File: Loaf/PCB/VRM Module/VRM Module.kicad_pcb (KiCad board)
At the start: 2 copper layers, 7 parts, among them U1 TPS564242DRLR

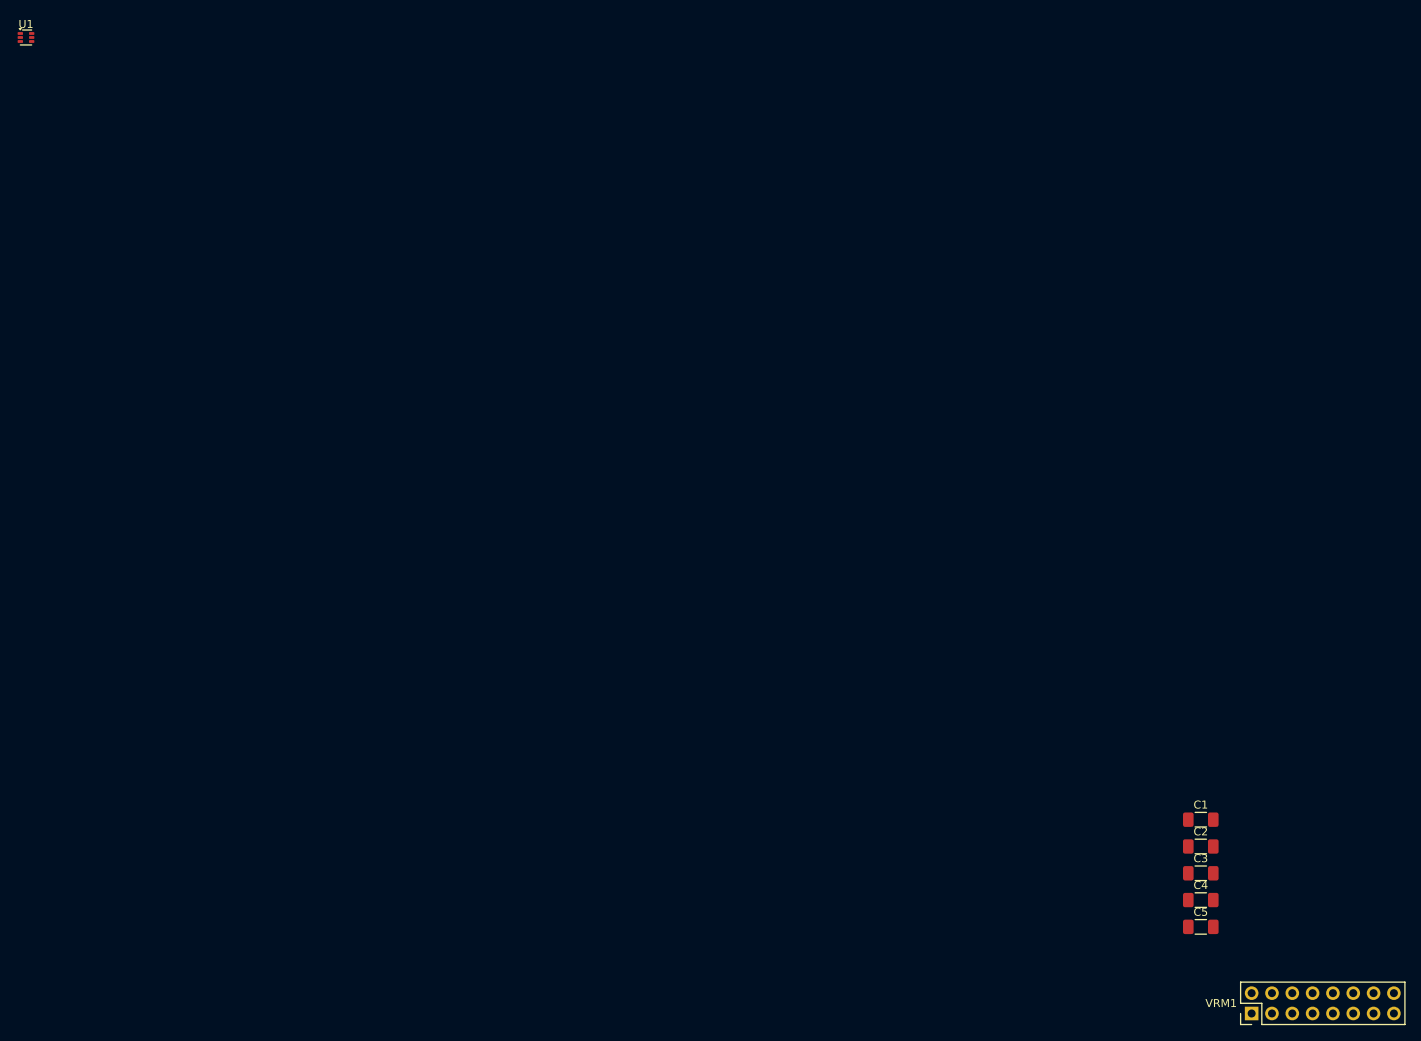
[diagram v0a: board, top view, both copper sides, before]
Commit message: IO PCB redesign progress upload
Switching to pi pico for better performance and to keep UART interface
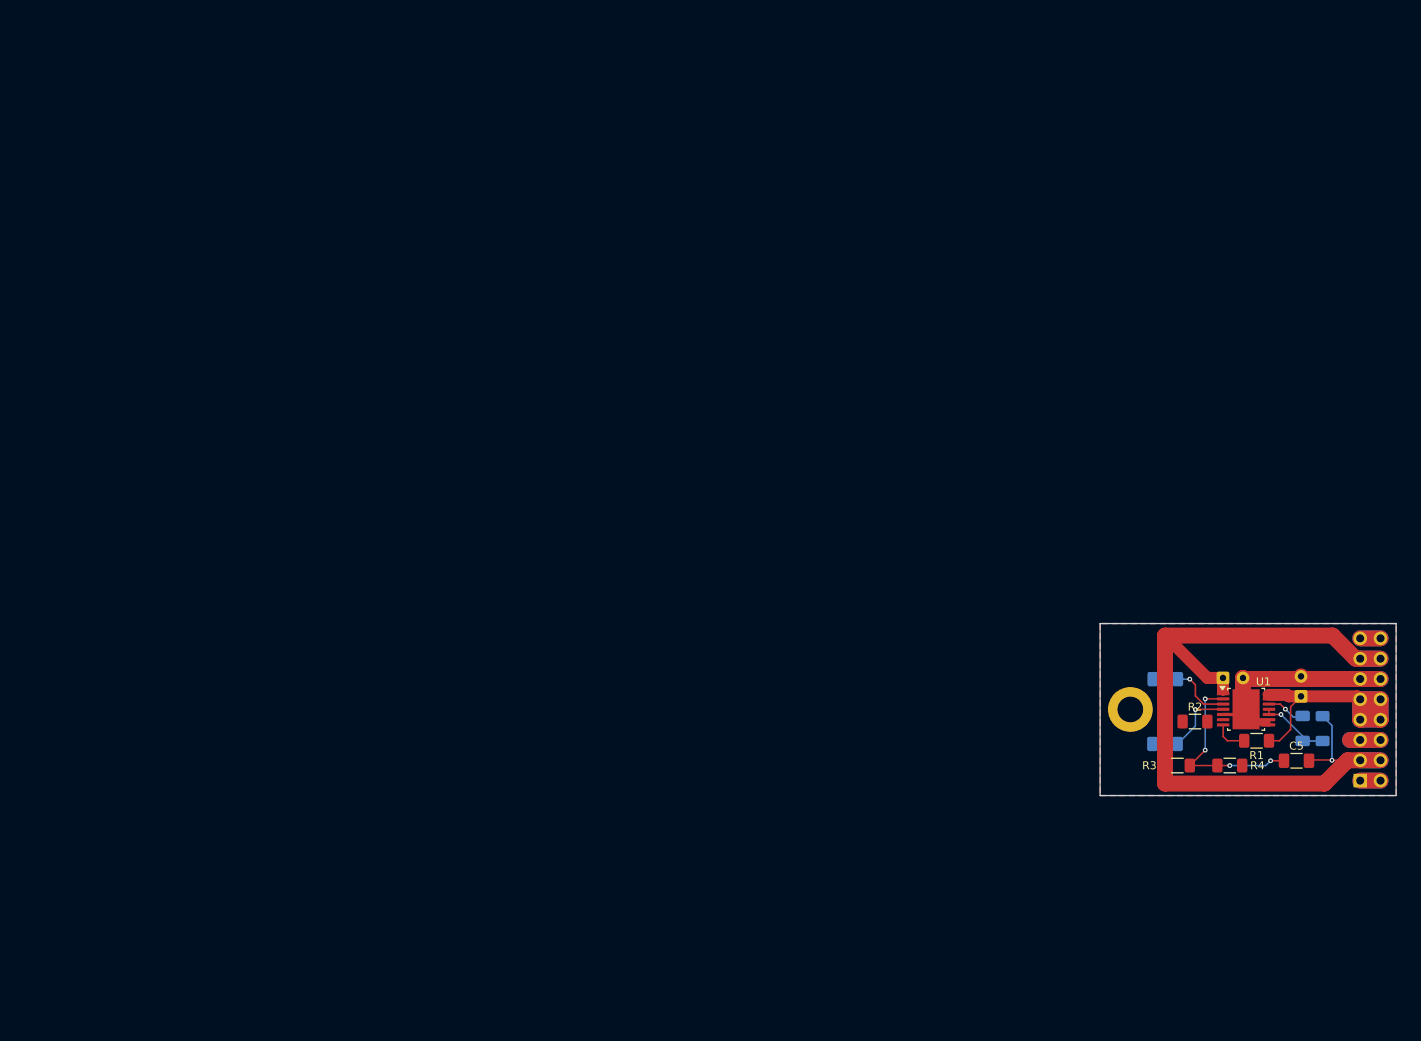
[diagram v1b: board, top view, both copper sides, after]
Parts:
- removed VRM1: VRM, Connector_PinHeader_2.54mm:PinHeader_2x08_P2.54mm_Vertical
- added C6: 22uF, Capacitor_THT:CP_Radial_D5.0mm_P2.50mm, B.Cu at (150.8, 81.2)
- added H1: MountingHole_Pad, MountingHole:MountingHole_3.2mm_M3_DIN965_Pad, B.Cu at (139.3, 85.2)
- added J1: VRM Pin Header, Connector_PinHeader_2.54mm:PinHeader_2x08_P2.54mm_Vertical, B.Cu at (168.0, 94.1)
- added L1: 3.3uH, Resistor_SMD:R_1206_3216Metric_Pad1.30x1.75mm_HandSolder, B.Cu at (163.3, 87.6)
- added R1: 10k, Resistor_SMD:R_1206_3216Metric_Pad1.30x1.75mm_HandSolder, F.Cu at (155.1, 89.1)
- added R2: 105k, Resistor_SMD:R_1206_3216Metric_Pad1.30x1.75mm_HandSolder, F.Cu at (147.3, 86.7)
- added R3: 133k, Resistor_SMD:R_1206_3216Metric_Pad1.30x1.75mm_HandSolder, F.Cu at (145.2, 92.2)
- added R4: 24k, Resistor_SMD:R_1206_3216Metric_Pad1.30x1.75mm_HandSolder, F.Cu at (151.7, 92.2)
- C1: footprint Capacitor_SMD:C_1206_3216Metric_Pad1.33x1.80mm_HandSolder -> Capacitor_THT:CP_Radial_D5.0mm_P2.50mm; moved to B.Cu
- C2: value 100nF -> 1uF; moved to B.Cu
- C3: value 33pF -> 3.3uF; moved to B.Cu
- C4: value 22uF -> 100nF; moved to B.Cu
- C5: value 100nF -> 10pF
- U1: value TPS564242DRLR -> TPS54429PWP; footprint Package_TO_SOT_SMD:SOT-563 -> Package_SO:Texas_HTSSOP-14-1EP_4.4x5mm_P0.65mm_EP3.4x5mm_Mask2.94x3.34mm
- moved U1 174.1 mm to (153.7, 85.2)
- moved C4 24.9 mm to (160.8, 87.6), turned to -90 degrees
- moved C5 24.0 mm to (160.0, 91.6)
- moved C2 21.4 mm to (143.6, 81.4)
- moved C1 19.9 mm to (160.6, 83.5), turned to 90 degrees
- moved C3 16.8 mm to (143.6, 89.5)
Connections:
- C2 pad 1: +12V -> GND
- C2 pad 2: GND -> /VREG
- C3 pad 1: +5V -> GND
- C3 pad 2: /FB -> Net-(U1-SS)
- C4 pad 1: +5V -> Net-(U1-VBST)
- C4 pad 2: GND -> Net-(U1-SW1)
- C5 pad 1: +5V -> /VFB
- C5 pad 2: GND -> +5V
- U1 pad 1: +12V -> +5V
- U1 pad 2: Net-(U1-SW) -> /VFB
- U1 pad 3: GND -> /VREG
- U1 pad 4: GND -> Net-(U1-SS)
- U1 pad 5: /EN -> GND
- U1 pad 6: /FB -> Net-(U1-PG)
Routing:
- net +5V: track 0.00 -> 103.2 mm, vias 0 -> 1
- net +12V: track 0.00 -> 47.2 mm
- net GND: track 0.00 -> 46.3 mm
- net /VFB: track 0.00 -> 23.4 mm, vias 0 -> 4
- net +3.3V: track 0.00 -> 10.2 mm
- net Net-(U1-SW1): track 0.00 -> 9.08 mm, vias 0 -> 1
- net Net-(U1-SS): track 0.00 -> 8.71 mm, vias 0 -> 1
- net /VREG: track 0.00 -> 7.78 mm, vias 0 -> 1
- net Net-(U1-VBST): track 0.00 -> 4.85 mm, vias 0 -> 1
- net Net-(U1-EN): track 0.00 -> 4.30 mm
- added copper zone on B.Cu, net GND
- added copper zone on F.Cu, net GND
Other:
- board outline added: 37 x 21.5 mm

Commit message: Updated DRC to fit new OSHE specs
pain
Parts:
- C2: moved to F.Cu
- moved C2 2.62 mm to (146.2, 81.2), turned to -90 degrees
- moved C6 2.25 mm to (150.8, 79.0)
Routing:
- net +5V: track 103.2 -> 100.4 mm
- net GND: track 46.3 -> 48.9 mm, vias 0 -> 1
- net Net-(U1-PG): track 0.00 -> 2.07 mm
- net /VREG: track 7.78 -> 9.11 mm, vias 1 -> 0
